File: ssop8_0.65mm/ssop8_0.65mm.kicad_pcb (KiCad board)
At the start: 2 copper layers, 10.8 x 5.1 mm, 1 part

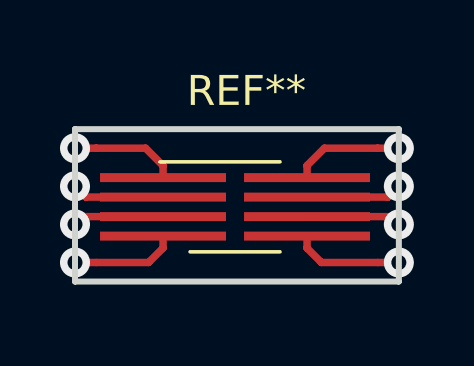
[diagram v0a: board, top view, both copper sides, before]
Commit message: Adding SSOP8 board.
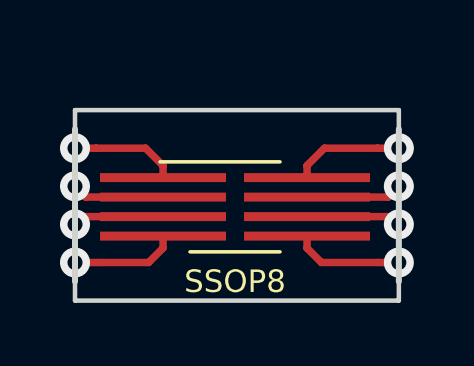
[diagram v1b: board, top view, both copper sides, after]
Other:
- board size 10.8 x 5.1 mm -> 10.8 x 6.3 mm
- board text added: "Cast. SSOP8 Breakout @coddingtonbear 25 Nov 2017 0.65mm Pitch Max 9mm Width"
- board text added: "SSOP8"
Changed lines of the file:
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@@
   (general
     (thickness 1.6)
-    (drawings 4)
+    (drawings 10)
     (tracks 32)
     (zones 0)
@@
     (tags "SSOP-8 2.95x2.8mm Pitch 0.65mm")
     (attr smd)
-    (fp_text reference REF** (at 0.381 -3.86) (layer F.SilkS)
+    (fp_text reference REF** (at 0.381 -4.495 180) (layer F.Fab)
       (effects (font (size 1 1) (thickness 0.15)))
     )
-    (fp_text value SSOP8 (at 0 3.76) (layer F.Fab)
+    (fp_text value SSOP8 (at 0 4.395) (layer F.Fab)
       (effects (font (size 1 1) (thickness 0.15)))
     )
@@
     (pad 1 smd rect (at -2.4 -0.975 270) (size 0.3 4.2) (layers F.Cu F.Paste F.Mask))
   )
+  (gr_text "Cast. SSOP8 Breakout\n@coddingtonbear\n25 Nov 2017\n\n0.65mm Pitch\nMax 9mm Width" (at 144.0815 85.9155) (layer B.SilkS)
+    (effects (font (size 0.5 0.5) (thickness 0.125)) (justify right mirror))
+  )
+  (gr_text SSOP8 (at 148.844 88.9) (layer F.SilkS)
+    (effects (font (size 0.75 0.75) (thickness 0.1875)))
+  )
+  (gr_line (start 143.51 89.535) (end 143.51 88.9) (layer Edge.Cuts) (width 0.15))
+  (gr_line (start 154.305 89.535) (end 143.51 89.535) (layer Edge.Cuts) (width 0.15))
+  (gr_line (start 154.305 83.82) (end 154.305 89.535) (layer Edge.Cuts) (width 0.15))
+  (gr_line (start 154.305 83.185) (end 154.305 83.82) (layer Edge.Cuts) (width 0.15))
+  (gr_line (start 143.51 83.185) (end 154.305 83.185) (layer Edge.Cuts) (width 0.15))
+  (gr_line (start 143.51 83.82) (end 143.51 83.185) (layer Edge.Cuts) (width 0.15))
   (gr_line (start 143.51 88.9) (end 143.51 83.82) (layer Edge.Cuts) (width 0.2))
-  (gr_line (start 154.305 88.9) (end 143.51 88.9) (layer Edge.Cuts) (width 0.2))
   (gr_line (start 154.305 83.82) (end 154.305 88.9) (layer Edge.Cuts) (width 0.2))
-  (gr_line (start 143.51 83.82) (end 154.305 83.82) (layer Edge.Cuts) (width 0.2))
   (segment (start 146.444 85.435) (end 146.444 85.035) (width 0.25) (layer F.Cu) (net 0))
   (segment (start 144.217106 84.455) (end 143.51 84.455) (width 0.25) (layer F.Cu) (net 0))
